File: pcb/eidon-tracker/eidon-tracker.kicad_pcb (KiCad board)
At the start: 2 copper layers, 29.5 x 24.2 mm, 3 parts, among them SW1 SS-12D00-G 4 E, U1 XIAO-ESP32C6, U2 GY-BNO085

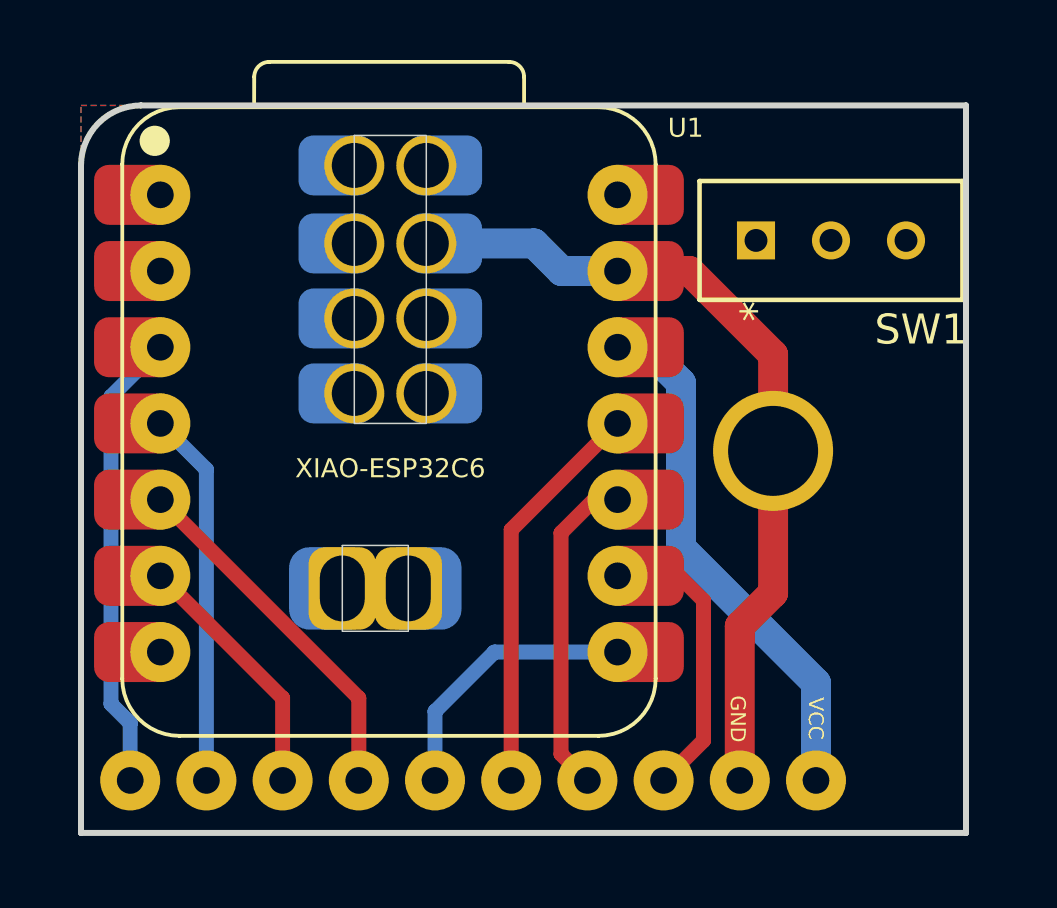
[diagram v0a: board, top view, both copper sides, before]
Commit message: feat(pcb): implements battery connector and power switch toggle
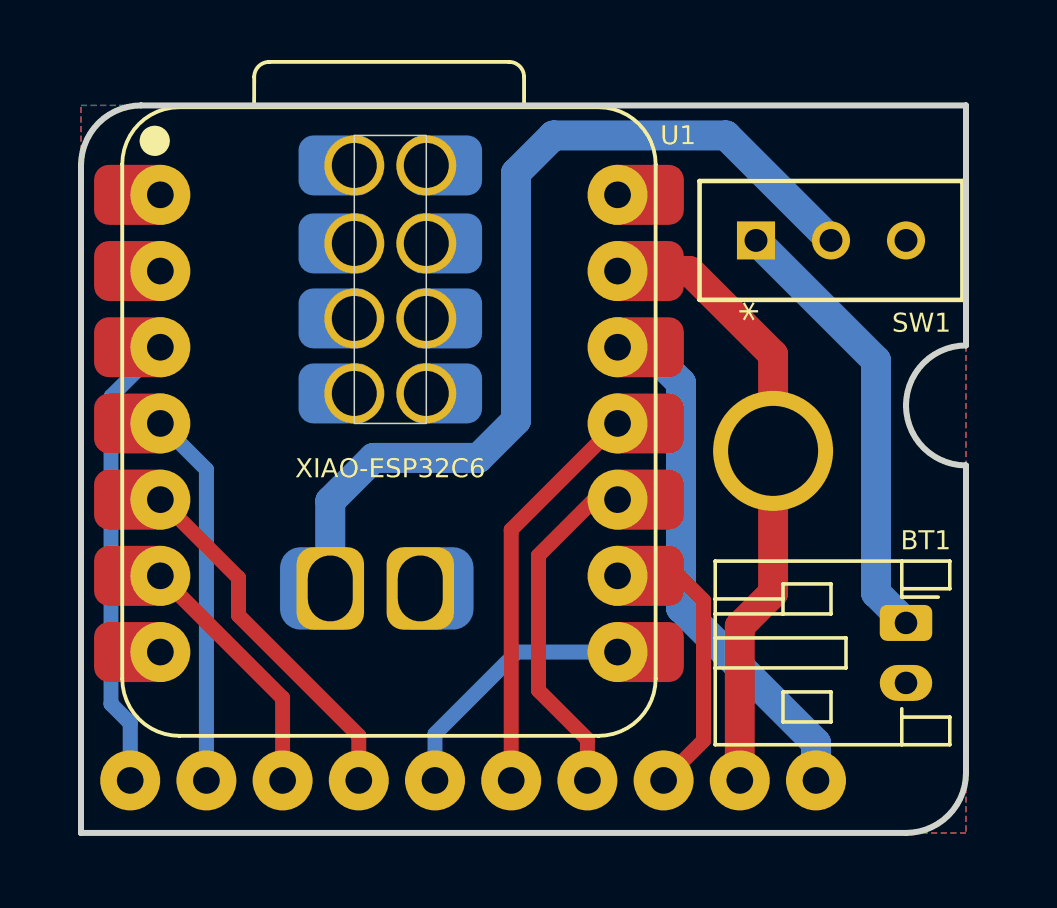
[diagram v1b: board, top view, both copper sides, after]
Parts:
- added BT1: Battery, Connector_JST:JST_PH_S2B-PH-K_1x02_P2.00mm_Horizontal, F.Cu at (161.5, 104.5)
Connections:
- SW1 pad 1: unconnected-(SW1-Pad1) -> /BAT0
- SW1 pad 2: unconnected-(SW1-Pad2) -> /BAT1
- U1 pad 15: unconnected-(U1-BAT-Pad15) -> /BAT1
- U1 pad 16: unconnected-(U1-GND-Pad16) -> GND
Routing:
- net /BAT1: track 0.00 -> 30.9 mm
- net /BAT0: track 0.00 -> 14.8 mm
- net GND: track 26.7 -> 21.0 mm
- net /MISO: track 11.0 -> 11.6 mm
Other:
- outline, holes or cut-outs redrawn

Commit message: feat(pcb): implements battery charging circuit and optimizes esp32-c6 footprint for what is needed
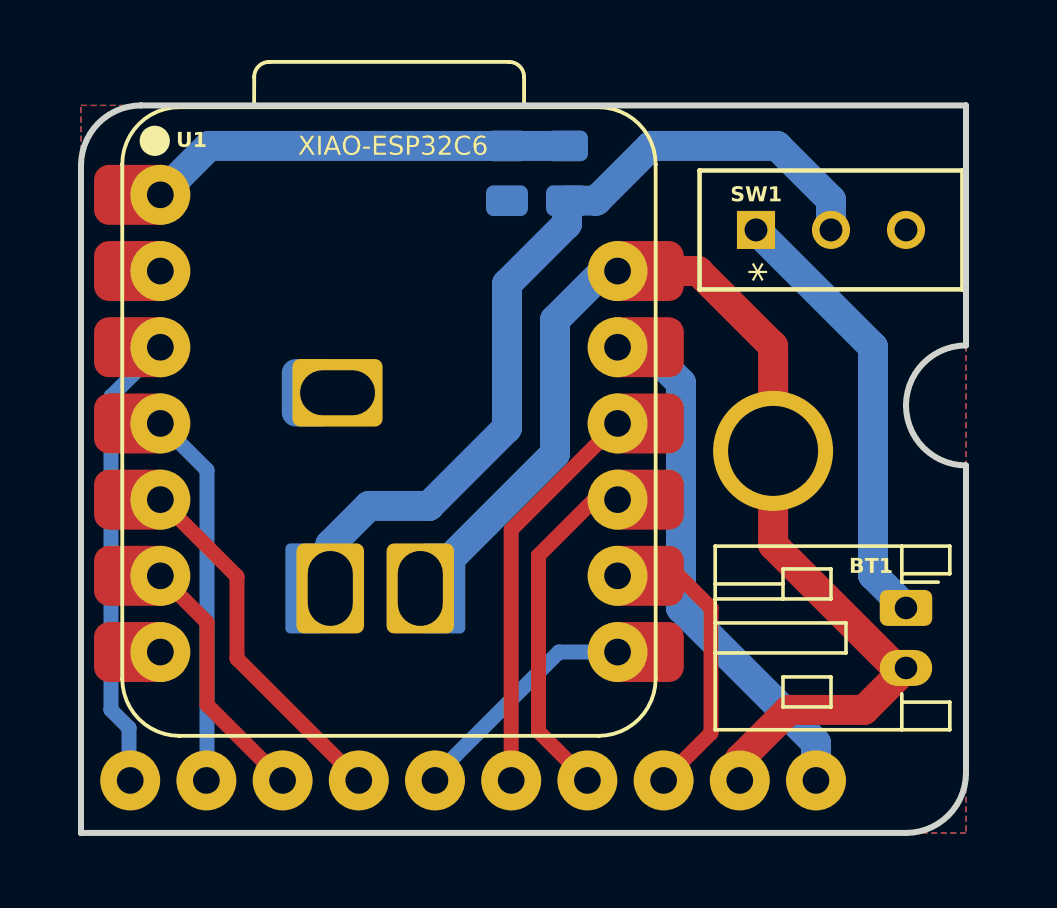
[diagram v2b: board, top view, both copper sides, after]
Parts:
- added R1: 220k, Resistor_SMD:R_0805_2012Metric, B.Cu at (150.2, 89.5)
- added R2: 220k, Resistor_SMD:R_0805_2012Metric, B.Cu at (148.2, 89.5)
- moved BT1 0.50 mm to (161.5, 104.0)
- moved SW1 0.35 mm to (156.5, 91.4)
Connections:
- U1 pad 1: unconnected-(U1-GPIO0_A0_D0-Pad1) -> /BAT
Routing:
- net GND: track 21.0 -> 40.1 mm
- net /BAT: track 0.00 -> 14.2 mm
- net /BAT1: track 30.9 -> 28.7 mm
- net /CS: track 8.77 -> 7.95 mm

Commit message: feat(pcb): further optimizations to PCB layout and implements boot/user button
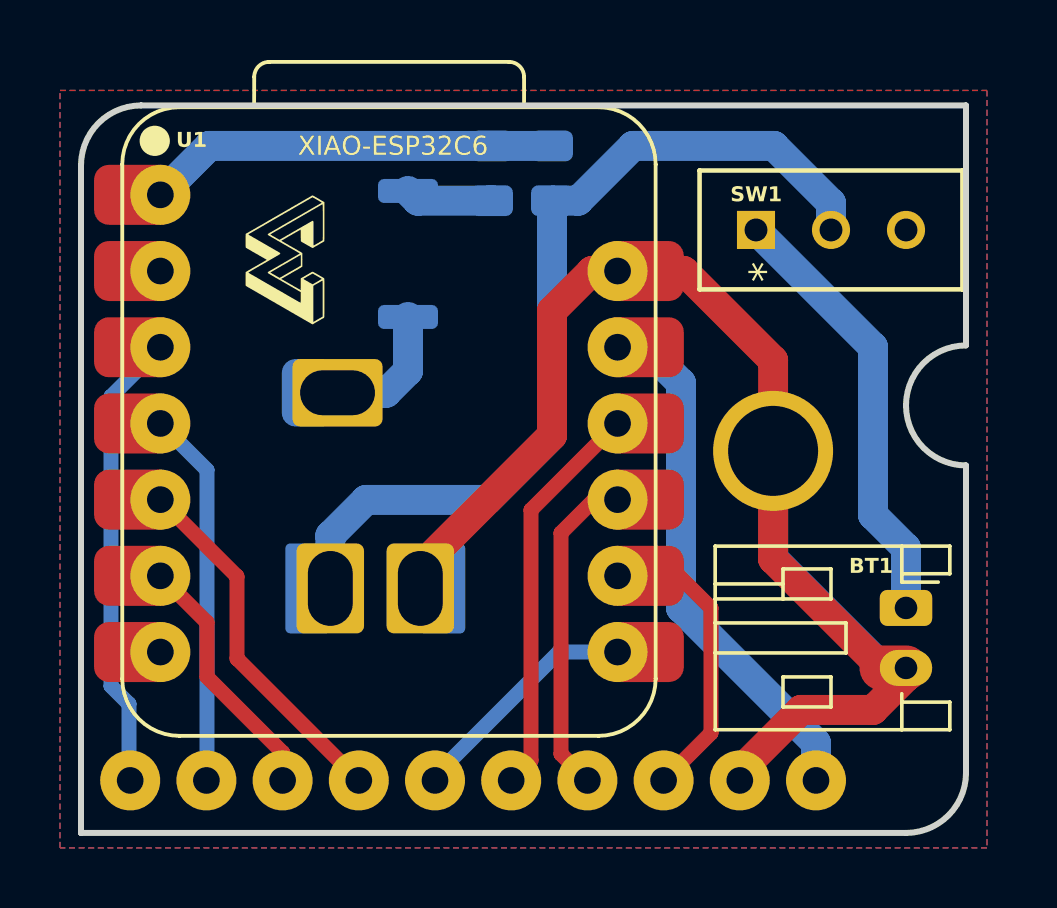
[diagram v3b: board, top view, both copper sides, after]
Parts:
- added G1: LOGO, LOGO, F.Cu at (140.8, 92.4)
- added SW2: SW_Push, Button_Switch_SMD:SW_Push_SPST_NO_Alps_SKRK, B.Cu at (144.9, 92.2)
- SW1: value SS-12D00-G 4 E -> SS12D00
- moved R1 0.50 mm to (149.7, 89.5)
- moved R2 0.50 mm to (147.7, 89.5)
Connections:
- net /BAT renamed /BAT_LVL
- BT1 pad 1: /BAT0 -> /BAT1
- R1 pad 2: /BAT1 -> /BAT2
- SW1 pad 1: /BAT0 -> /BAT1
- SW1 pad 2: /BAT1 -> /BAT2
- U1 pad 15: /BAT1 -> /BAT2
- U1 pad 23: unconnected-(U1-BOOT-Pad23) -> /BOOT
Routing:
- net /BAT2: track 0.00 -> 30.1 mm
- net /BAT0: track 14.7 -> 0.00 mm
- net /BAT1: track 28.7 -> 14.7 mm
- net GND: track 40.1 -> 53.2 mm
- net /BOOT: track 0.00 -> 4.93 mm
- net /MISO: track 11.6 -> 11.0 mm
- net /BAT_LVL: track 14.2 -> 13.7 mm

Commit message: feat(pcb): implements button and led circuit with smd componenets; chore(pcb): cleans up schematic and adds group labels to make the parts easier to understand
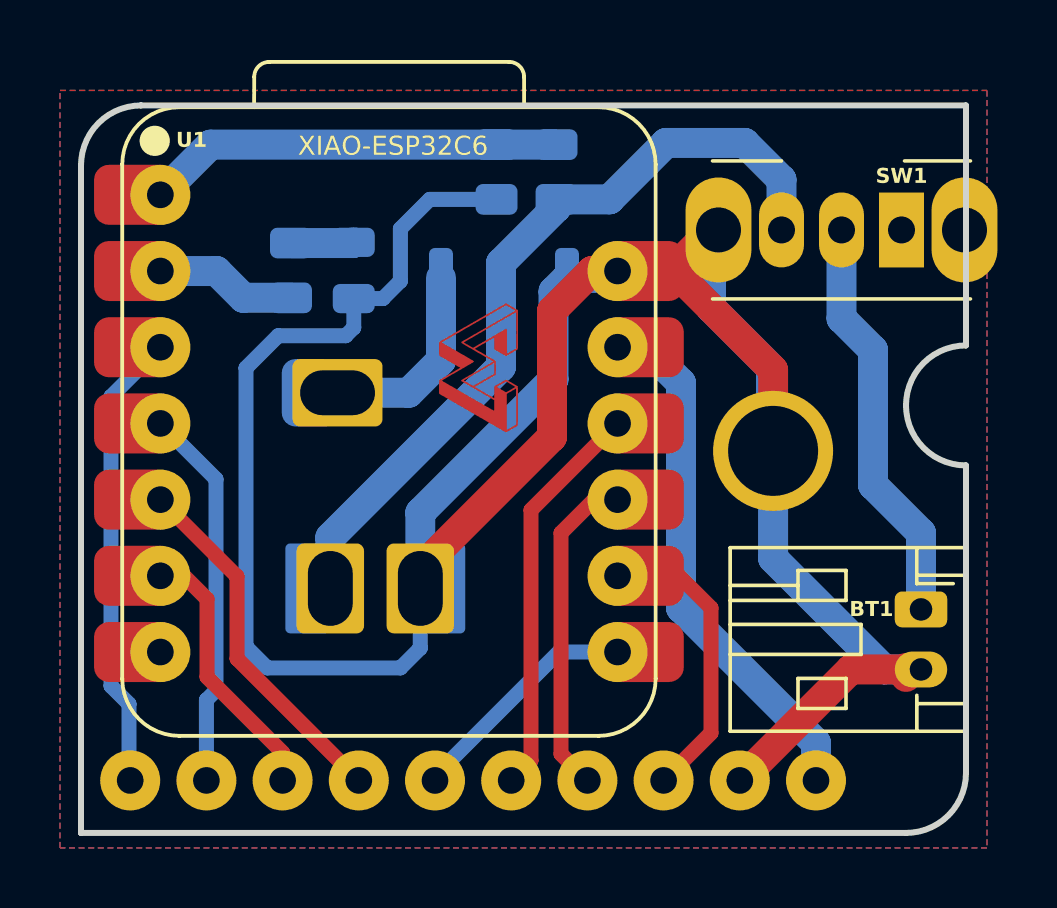
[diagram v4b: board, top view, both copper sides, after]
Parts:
- added D1: LED, LED_SMD:LED_0805_2012Metric, B.Cu at (143.1, 92.8)
- added G1: LOGO, LOGO, F.Cu at (147.2, 96.0)
- added R3: 1.8k, Resistor_SMD:R_0805_2012Metric, B.Cu at (141.0, 92.8)
- G1: moved to B.Cu
- SW1: value SS12D00 -> SW_SPDT; footprint eidon-tracker:1P2T_SS-12D00_CNK -> eidon-tracker:SW_Slide_SPDT_Angled_CK_OS102011MA1Q
- moved G1 26.3 mm to (161.4, 108.8), turned to 180 degrees
- moved SW1 4.85 mm to (161.3, 91.4), turned to 180 degrees
- moved SW2 3.30 mm to (148.1, 93.0), turned to 0 degrees
- moved BT1 0.50 mm to (162.0, 104.0)
- moved R1 0.16 mm to (149.9, 89.5)
- moved R2 0.16 mm to (147.9, 89.5)
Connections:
- BT1 pad 1: /BAT1 -> /BAT_EXT
- R1 pad 2: /BAT2 -> /BAT_INT
- SW1 pad 1: /BAT1 -> unconnected-(SW1-A-Pad1)
- SW1 pad 2: /BAT2 -> /BAT_EXT
- SW1 pad 3: unconnected-(SW1-Pad3) -> /BAT_INT
- U1 pad 15: /BAT2 -> /BAT_INT
- U1 pad 2: unconnected-(U1-GPIO1_A1_D1-Pad2)_1 -> /LED
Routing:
- net GND: track 53.2 -> 97.9 mm
- net /BAT2: track 30.1 -> 0.00 mm
- net /BAT_INT: track 0.00 -> 26.6 mm
- net /BAT1: track 14.7 -> 0.00 mm
- net /BAT_EXT: track 0.00 -> 13.7 mm
- net /LED: track 0.00 -> 4.72 mm
- net Net-(D1-A): track 0.00 -> 2.14 mm
- net /BOOT: track 4.93 -> 6.65 mm
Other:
- board text added: "EIDON-TRACKER V03"
- board text added: "EIDON.AI©️2025"

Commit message: feat(pcb): adds vias to create better connected ground planes; rotates batery connector to make it easier to plug-in the battery
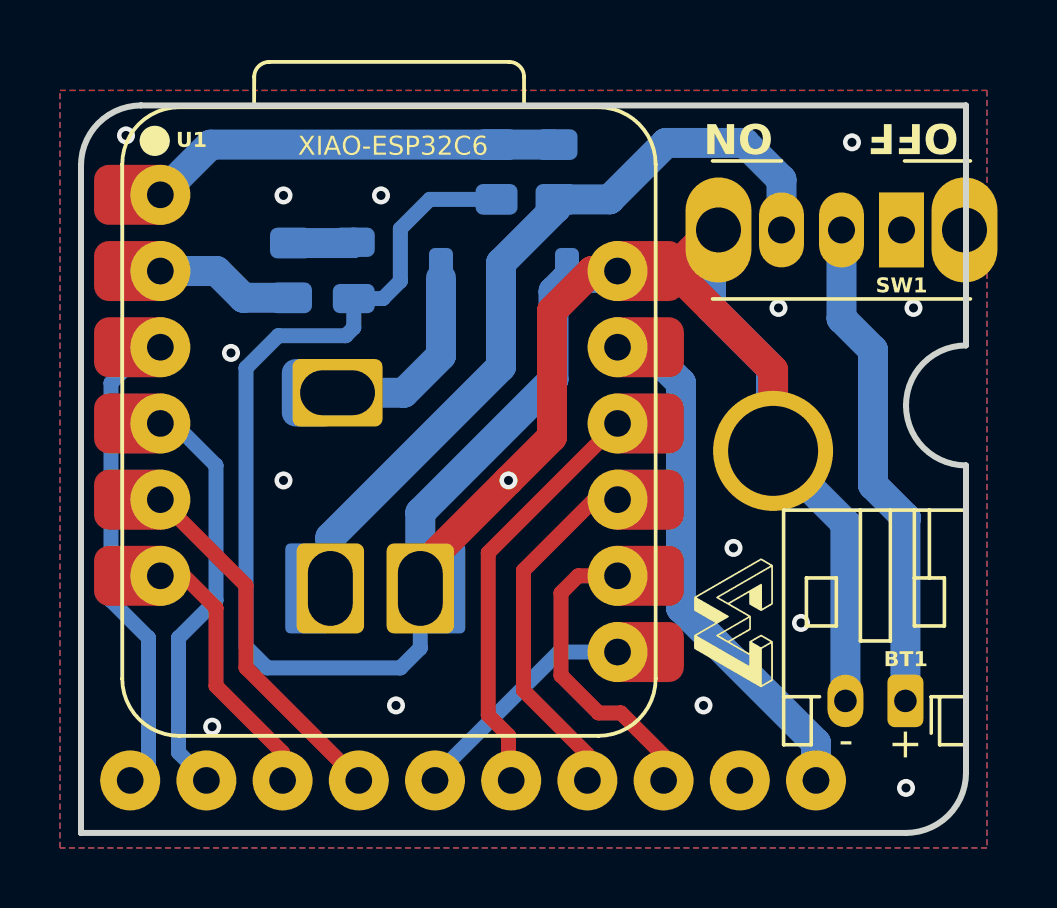
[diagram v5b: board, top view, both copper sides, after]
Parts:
- G1: moved to F.Cu
- G1: moved to B.Cu
- moved G1 15.8 mm to (161.5, 102.8), turned to 180 degrees
- moved G1 7.03 mm to (155.8, 104.5), turned to 0 degrees
- moved BT1 3.09 mm to (161.5, 107.1), turned to 180 degrees
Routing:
- net GND: track 97.9 -> 89.3 mm, vias 0 -> 15
- net /BAT_EXT: track 13.7 -> 16.6 mm
- net /PS1: track 12.8 -> 13.8 mm
- net /MISO: track 11.0 -> 12.0 mm
- net /PS0: track 15.4 -> 16.2 mm
- net /MOSI: track 13.4 -> 14.0 mm
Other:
- board text added: "OFF"
- board text added: "ON"

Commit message: feat(pcb): generates gerber files for fabrication
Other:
- rule pad_to_mask_clearance: 0 -> 0.05
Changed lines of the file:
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@@
 	)
 	(setup
-		(pad_to_mask_clearance 0)
+		(pad_to_mask_clearance 0.05)
+		(solder_mask_min_width 0.05)
 		(allow_soldermask_bridges_in_footprints no)
 		(tenting front back)
@@
 			(plot_on_all_layers_selection 0x00000000_00000000_00000000_00000000)
 			(disableapertmacros no)
-			(usegerberextensions no)
-			(usegerberattributes yes)
-			(usegerberadvancedattributes yes)
-			(creategerberjobfile yes)
+			(usegerberextensions yes)
+			(usegerberattributes no)
+			(usegerberadvancedattributes no)
+			(creategerberjobfile no)
 			(dashed_line_dash_ratio 12.000000)
 			(dashed_line_gap_ratio 3.000000)
@@
 			(sketchdnponfab yes)
 			(crossoutdnponfab yes)
-			(subtractmaskfromsilk no)
+			(subtractmaskfromsilk yes)
 			(outputformat 1)
 			(mirror no)
-			(drillshape 1)
+			(drillshape 0)
 			(scaleselection 1)
-			(outputdirectory "")
+			(outputdirectory "gerbers/")
 		)
 	)
@@
 		)
 		(fp_text user "-"
-			(at 1.98 -0.9 -180)
+			(at 1.98 -0.9 180)
 			(unlocked yes)
 			(layer "F.SilkS")
@@
 		)
 		(fp_text user "+"
-			(at 0 -0.9 -180)
-			(unlocked yes)
-			(layer "F.SilkS")
+			(at 0 -0.9 180)
+			(unlocked yes)
+			(layer "F.SilkS")

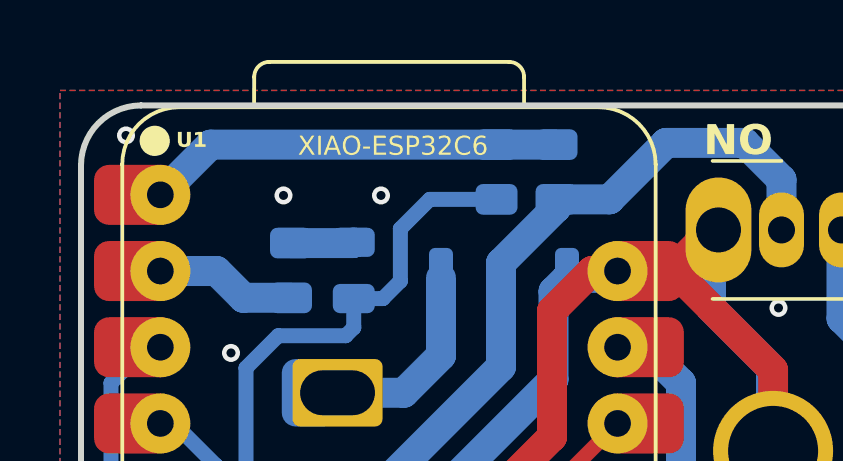
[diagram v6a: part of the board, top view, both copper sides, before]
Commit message: feat(pcb): adds BOM and pick-n-place pos files needed for PCBA
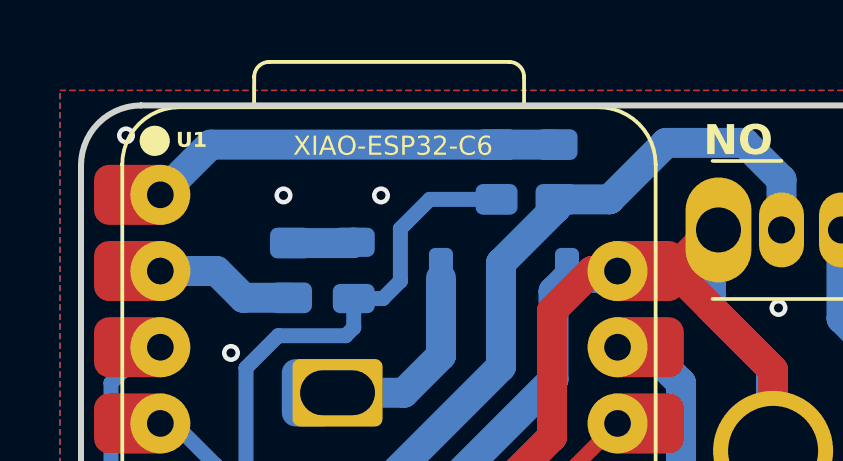
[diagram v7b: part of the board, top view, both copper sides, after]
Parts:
- U1: value XIAO-ESP32C6 -> XIAO-ESP32-C6
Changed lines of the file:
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@@
 			)
 		)
-		(property "Value" "XIAO-ESP32C6"
+		(property "Value" "XIAO-ESP32-C6"
 			(at 0.09 -9.25 0)
 			(unlocked yes)
@@
 			)
 		)
+		(property "Manufacturer" "Seeed / Digi-Key"
+			(at 0 0 0)
+			(unlocked yes)
+			(layer "F.Fab")
+			(hide yes)
+			(effects
+				(font
+					(size 1 1)
+					(thickness 0.15)
+				)
+			)
+		)
+		(property "MPN" "Seeed 113991114"
+			(at 0 0 0)
+			(unlocked yes)
+			(layer "F.Fab")
+			(hide yes)
+			(effects
+				(font
+					(size 1 1)
+					(thickness 0.15)
+				)
+			)
+		)
+		(property "Supplier" "Seeed / Digi-Key"
+			(at 0 0 0)
+			(unlocked yes)
+			(layer "F.Fab")
+			(hide yes)
+			(effects
+				(font
+					(size 1 1)
+					(thickness 0.15)
+				)
+			)
+		)
+		(property "Description" "XIAO-ESP32C6 MCU Module"
+			(at 0 0 0)
+			(unlocked yes)
+			(layer "F.Fab")
+			(hide yes)
+			(effects
+				(font
+					(size 1 1)
+					(thickness 0.15)
+				)
+			)
+		)
 		(sheetname "/")
 		(sheetfile "eidon-tracker.kicad_sch")
-		(attr through_hole)
+		(attr through_hole dnp)
 		(fp_line
 			(start -8.935 8.509)
@@
 		(sheetname "/")
 		(sheetfile "eidon-tracker.kicad_sch")
-		(attr through_hole)
+		(attr through_hole dnp)
 		(fp_line
 			(start 7.5 -12.7)
